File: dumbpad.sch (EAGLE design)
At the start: 42 parts

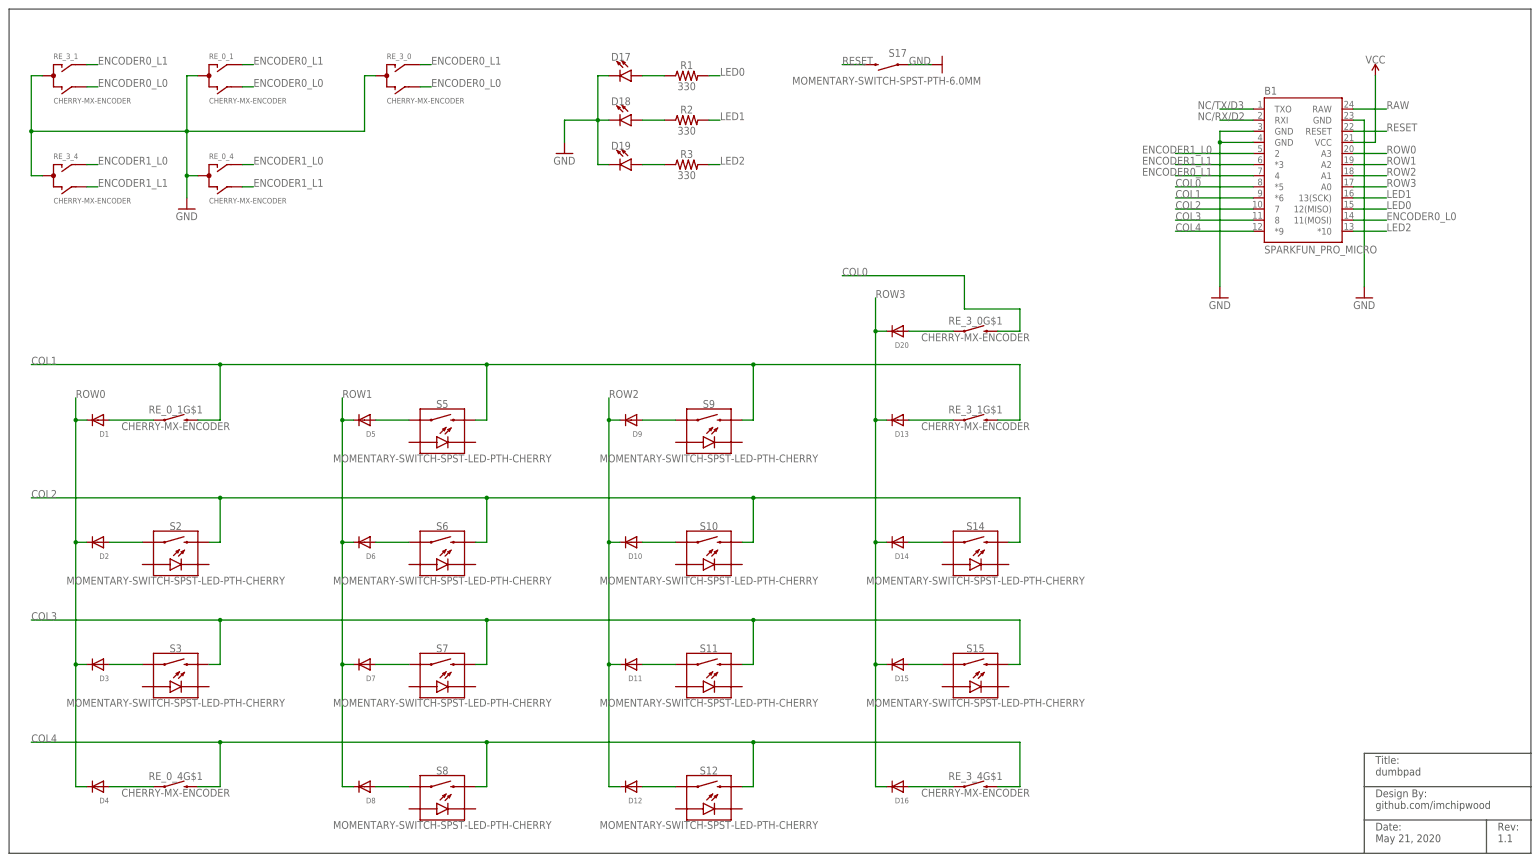
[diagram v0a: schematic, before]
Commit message: made a version that uses Teensy 2.0
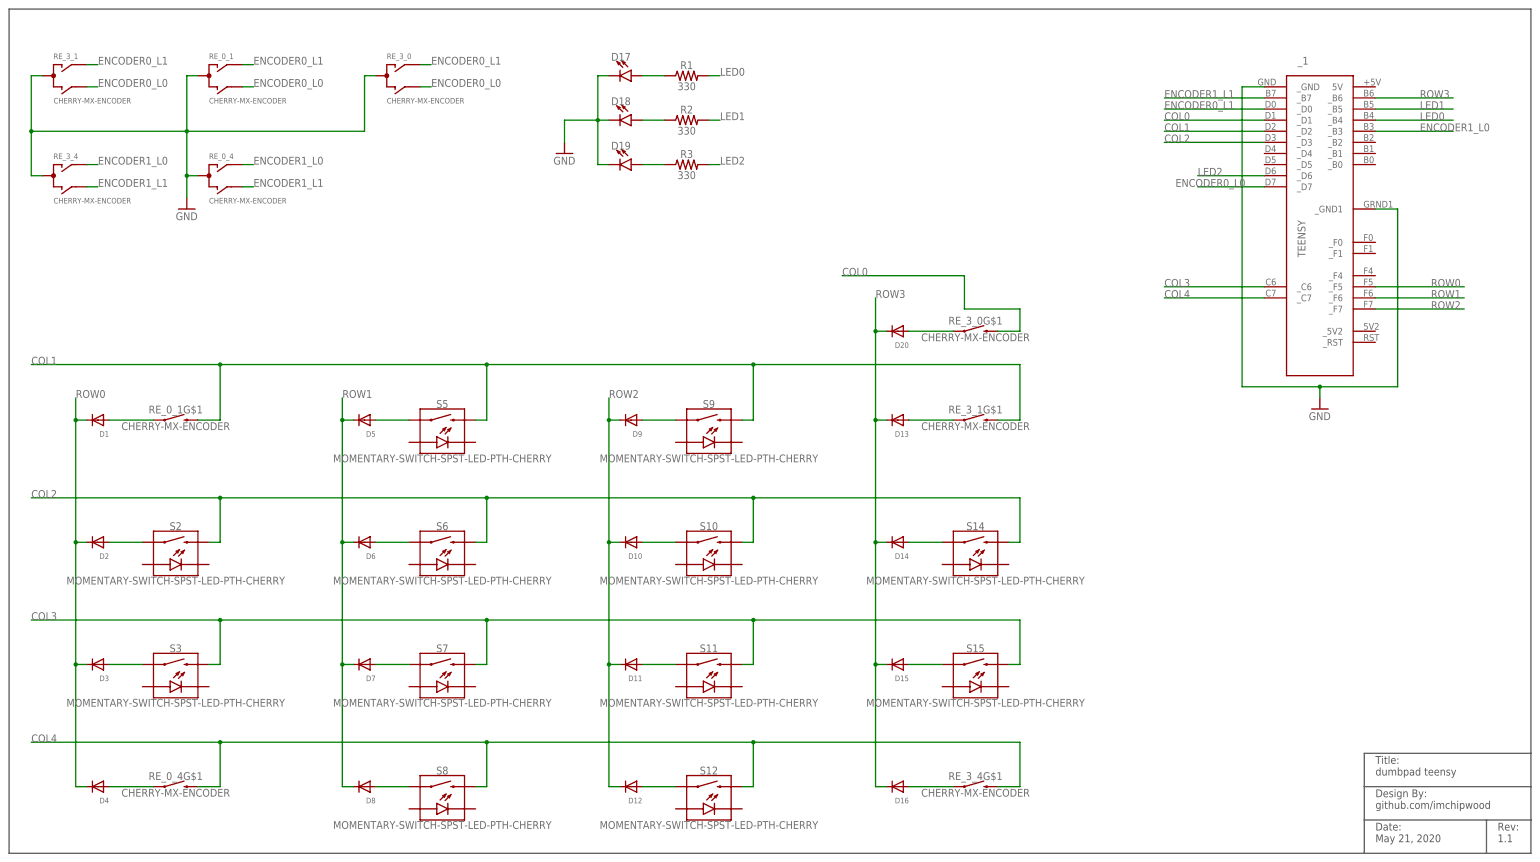
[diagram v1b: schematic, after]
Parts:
- removed B1: SPARKFUN_PRO_MICRO, SparkFun-Boards:SPARKFUN_PRO_MICRO
- removed S17: MOMENTARY-SWITCH-SPST-PTH-6.0MM, SparkFun-Switches:MOMENTARY-SWITCH-SPST-PTH-6.0MM
- added _1: TEENSY, cpwood:TEENSY
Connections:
- removed net NC/RX/D2: B1.RXI
- removed net NC/TX/D3: B1.TXO
- removed net RAW: B1.RAW
- removed net RESET: B1.RESET, S17.2
- removed net VCC: B1.VCC
- net COL0: now also _1._D1; no longer B1.*5
- net COL1: now also _1._D2; no longer B1.*6
- net COL2: now also _1._D3; no longer B1.7
- net COL3: now also _1._C6; no longer B1.8
- net COL4: now also _1._C7; no longer B1.*9
- net ENCODER0_L0: now also _1._D7; no longer B1.11(MOSI)
- net ENCODER0_L1: now also _1._D0; no longer B1.4
- net ENCODER1_L0: now also _1._B3; no longer B1.2
- net ENCODER1_L1: now also _1._B7; no longer B1.*3
- net GND: now also _1._GND, _1._GND1; no longer B1.GND, B1.GND@1, B1.GND@2, S17.1
- net LED0: now also _1._B4; no longer B1.12(MISO)
- net LED1: now also _1._B5; no longer B1.13(SCK)
- net LED2: now also _1._D6; no longer B1.*10
- net ROW0: now also _1._F5; no longer B1.A3
- net ROW1: now also _1._F6; no longer B1.A2
- net ROW2: now also _1._F7; no longer B1.A1
- net ROW3: now also _1._B6; no longer B1.A0
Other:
- note added: "Title: dumbpad teensy"
- note removed: "Title: dumbpad"
